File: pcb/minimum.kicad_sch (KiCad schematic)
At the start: 38 parts, among them J1 DX07P024MJ1R1500, SW1 SW_Push, U1 RP2040, U2 SCD4x, U3 W25Q16JVUXIQ, U4 XCL220, Y1 C2E-12.000-18-1020-X-R

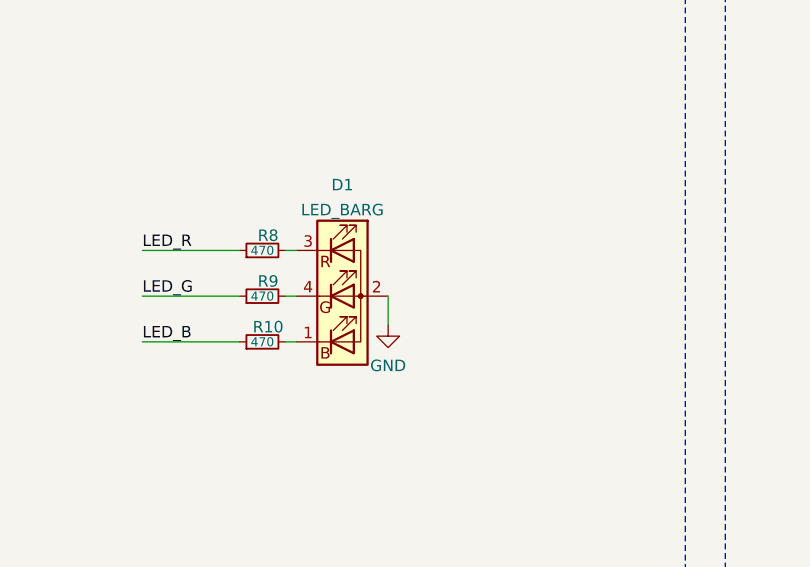
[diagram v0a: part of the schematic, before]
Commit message: Fix common pin RGB Led
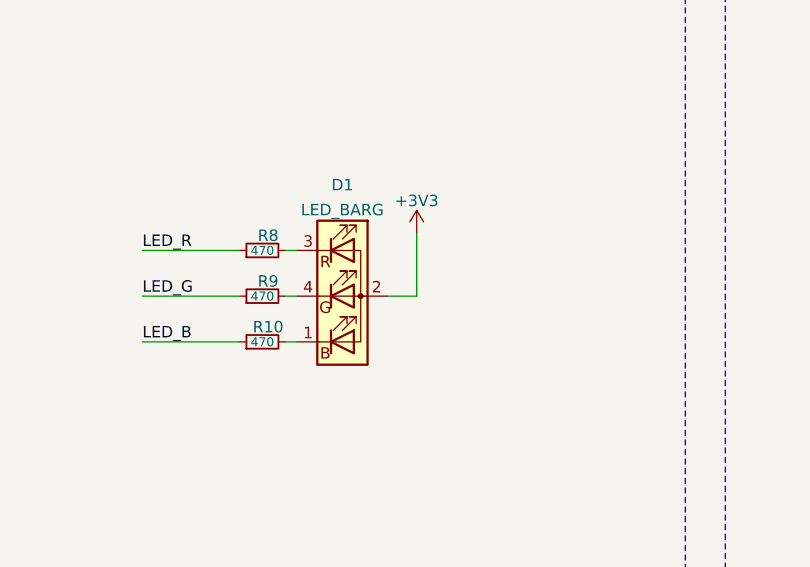
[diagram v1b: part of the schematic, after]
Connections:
- net +3V3: now also D1.2 (A)
- net GND: no longer D1.2 (A)
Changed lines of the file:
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@@
     (stroke (width 0) (type solid) (color 0 0 0 0))
   )
-  (wire (pts (xy 276.225 114.935) (xy 276.225 118.11))
+  (wire (pts (xy 276.225 114.935) (xy 279.4 114.935))
+    (stroke (width 0) (type solid) (color 0 0 0 0))
+  )
+  (wire (pts (xy 279.4 114.935) (xy 279.4 107.95))
     (stroke (width 0) (type solid) (color 0 0 0 0))
   )
@@
     (pin "1")
   )
+  (symbol (lib_id "power:+3V3") (at 279.4 107.95 0) (unit 1)
+    (in_bom yes) (on_board yes) (fields_autoplaced)
+    (property "Reference" "#PWR?" (id 0) (at 279.4 111.76 0)
+      (effects (font (size 1.27 1.27)) hide)
+    )
+    (property "Value" "+3V3" (id 1) (at 279.4 104.3454 0))
+    (property "Footprint" "" (id 2) (at 279.4 107.95 0)
+      (effects (font (size 1.27 1.27)) hide)
+    )
+    (property "Datasheet" "" (id 3) (at 279.4 107.95 0)
+      (effects (font (size 1.27 1.27)) hide)
+    )
+    (pin "1")
+  )
   (symbol (lib_id "power:VBUS") (at 295.91 46.355 0) (unit 1)
     (in_bom yes) (on_board yes) (fields_autoplaced)
@@
     )
     (property "Datasheet" "" (id 3) (at 276.225 64.135 0)
-      (effects (font (size 1.27 1.27)) hide)
-    )
-    (pin "1")
-  )
-  (symbol (lib_id "power:GND") (at 276.225 118.11 0) (unit 1)
-    (in_bom yes) (on_board yes) (fields_autoplaced)
-    (property "Reference" "#PWR0135" (id 0) (at 276.225 124.46 0)
-      (effects (font (size 1.27 1.27)) hide)
-    )
-    (property "Value" "GND" (id 1) (at 276.225 122.6726 0))
-    (property "Footprint" "" (id 2) (at 276.225 118.11 0)
-      (effects (font (size 1.27 1.27)) hide)
-    )
-    (property "Datasheet" "" (id 3) (at 276.225 118.11 0)
       (effects (font (size 1.27 1.27)) hide)
     )
@@
       (reference "#PWR0134") (unit 1) (value "GND") (footprint "")
     )
-    (path "/058a8eb3-978b-4028-916d-7a96a512f9f8"
-      (reference "#PWR0135") (unit 1) (value "GND") (footprint "")
+    (path "/e878188d-6393-45e3-a71a-8e9b2bb84959"
+      (reference "#PWR?") (unit 1) (value "+3V3") (footprint "")
     )
     (path "/e7effd1f-dcf0-44f9-acf3-2bc5919ae9df"
